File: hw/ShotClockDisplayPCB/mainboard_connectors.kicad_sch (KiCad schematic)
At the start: 1 part, among them U6 S6B-PH-K-S-(LF)(SN)

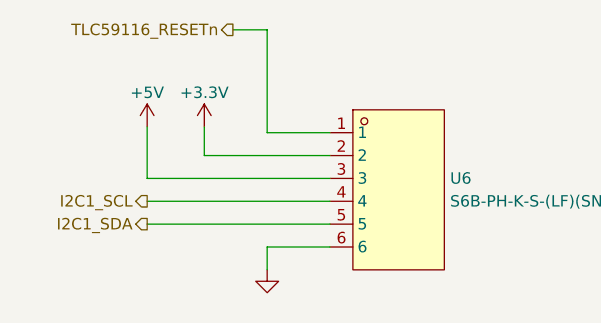
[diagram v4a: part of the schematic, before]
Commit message: Started on display board rework
added new footprints
added HW select shunts/jumpers
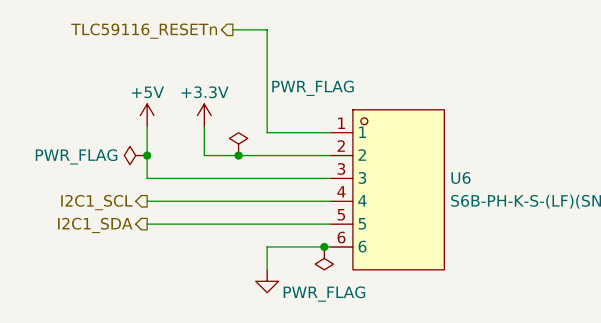
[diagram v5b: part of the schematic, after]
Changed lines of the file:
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@@
 (kicad_sch (version 20230121) (generator eeschema)
   (paper "A4")
-  (wire (pts (xy 121.285 80.01) (xy 135.255 80.01))
+  (junction (at 125.095 80.01) (diameter 0) (color 0 0 0 0)
+  )
+  (junction (at 134.62 90.17) (diameter 0) (color 0 0 0 0)
+  )
+  (junction (at 114.935 80.01) (diameter 0) (color 0 0 0 0)
+  )
+  (wire (pts (xy 121.285 80.01) (xy 125.095 80.01))
     (stroke (width 0) (type default))
   )
@@
     (stroke (width 0) (type default))
   )
-  (wire (pts (xy 135.255 90.17) (xy 128.27 90.17))
+  (wire (pts (xy 125.095 80.01) (xy 135.255 80.01))
     (stroke (width 0) (type default))
   )
-  (wire (pts (xy 114.935 82.55) (xy 114.935 76.835))
+  (wire (pts (xy 135.255 90.17) (xy 134.62 90.17))
+    (stroke (width 0) (type default))
+  )
+  (wire (pts (xy 114.935 82.55) (xy 114.935 80.01))
     (stroke (width 0) (type default))
   )
   (wire (pts (xy 121.285 80.01) (xy 121.285 76.835))
+    (stroke (width 0) (type default))
+  )
+  (wire (pts (xy 114.935 80.01) (xy 114.935 76.835))
     (stroke (width 0) (type default))
   )
@@
     (stroke (width 0) (type default))
   )
+  (wire (pts (xy 134.62 90.17) (xy 128.27 90.17))
+    (stroke (width 0) (type default))
+  )
   (hierarchical_label "I2C1_SDA" (shape output) (at 114.935 87.63 180) (fields_autoplaced)
     (effects (font (size 1.27 1.27)) (justify right))
@@
   (hierarchical_label "I2C1_SCL" (shape output) (at 114.935 85.09 180) (fields_autoplaced)
     (effects (font (size 1.27 1.27)) (justify right))
+  )
+  (symbol (lib_id "power:PWR_FLAG") (at 125.095 80.01 0) (unit 1)
+    (in_bom yes) (on_board yes) (dnp no)
+    (property "Reference" "#FLG03" (at 125.095 78.105 0)
+      (effects (font (size 1.27 1.27)) hide)
+    )
+    (property "Value" "PWR_FLAG" (at 133.35 72.39 0)
+      (effects (font (size 1.27 1.27)))
+    )
+    (property "Footprint" "" (at 125.095 80.01 0)
+      (effects (font (size 1.27 1.27)) hide)
+    )
+    (property "Datasheet" "~" (at 125.095 80.01 0)
+      (effects (font (size 1.27 1.27)) hide)
+    )
+    (pin "1")
+    (instances
+      (project "ShotClockDisplayPCB"
+        (path "/baf3f1b3-1588-4756-b7d1-50b7c58bafb0/acc83e16-b7da-48bd-ac1b-341a95513ee6"
+          (reference "#FLG03") (unit 1)
+        )
+      )
+    )
+  )
+  (symbol (lib_id "power:PWR_FLAG") (at 134.62 90.17 180) (unit 1)
+    (in_bom yes) (on_board yes) (dnp no) (fields_autoplaced)
+    (property "Reference" "#FLG02" (at 134.62 92.075 0)
+      (effects (font (size 1.27 1.27)) hide)
+    )
+    (property "Value" "PWR_FLAG" (at 134.62 95.25 0)
+      (effects (font (size 1.27 1.27)))
+    )
+    (property "Footprint" "" (at 134.62 90.17 0)
+      (effects (font (size 1.27 1.27)) hide)
+    )
+    (property "Datasheet" "~" (at 134.62 90.17 0)
+      (effects (font (size 1.27 1.27)) hide)
+    )
+    (pin "1")
+    (instances
+      (project "ShotClockDisplayPCB"
+        (path "/baf3f1b3-1588-4756-b7d1-50b7c58bafb0/acc83e16-b7da-48bd-ac1b-341a95513ee6"
+          (reference "#FLG02") (unit 1)
+        )
+      )
+    )
   )
   (symbol (lib_id "power:+3.3V") (at 121.285 76.835 0) (unit 1)
@@
         )
       )
+    )
+  )
+  (symbol (lib_id "power:PWR_FLAG") (at 114.935 80.01 90) (unit 1)
+    (in_bom yes) (on_board yes) (dnp no) (fields_autoplaced)
+    (property "Reference" "#FLG01" (at 113.03 80.01 0)
+      (effects (font (size 1.27 1.27)) hide)
+    )
+    (property "Value" "PWR_FLAG" (at 111.76 80.01 90)
+      (effects (font (size 1.27 1.27)) (justify left))
+    )
+    (property "Footprint" "" (at 114.935 80.01 0)
+      (effects (font (size 1.27 1.27)) hide)
+    )
+    (property "Datasheet" "~" (at 114.935 80.01 0)
+      (effects (font (size 1.27 1.27)) hide)
+    )
+    (pin "1")
+    (instances
+      (project "ShotClockDisplayPCB"
+        (path "/baf3f1b3-1588-4756-b7d1-50b7c58bafb0/acc83e16-b7da-48bd-ac1b-341a95513ee6"
+          (reference "#FLG01") (unit 1)
+        )
+      )
